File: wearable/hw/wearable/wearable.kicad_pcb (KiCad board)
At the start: 2 copper layers, 80.2 x 35 mm, 105 parts, among them IC1 LM4041CILPR, J2 Conn_02x05_Odd_Even, J3 Interrupts, J4 Data, J5 Data, J8 USBC Charger, SW1 SW_Toggle, U1 LT3042xMSE, U2 BNO080, U3 nRF54L15-QFXX, U4 MAX77659AENV+, U5 ADS1299IPAG, Y1 32MHz, Y2 32.768kHz, Y3 32.768kHz

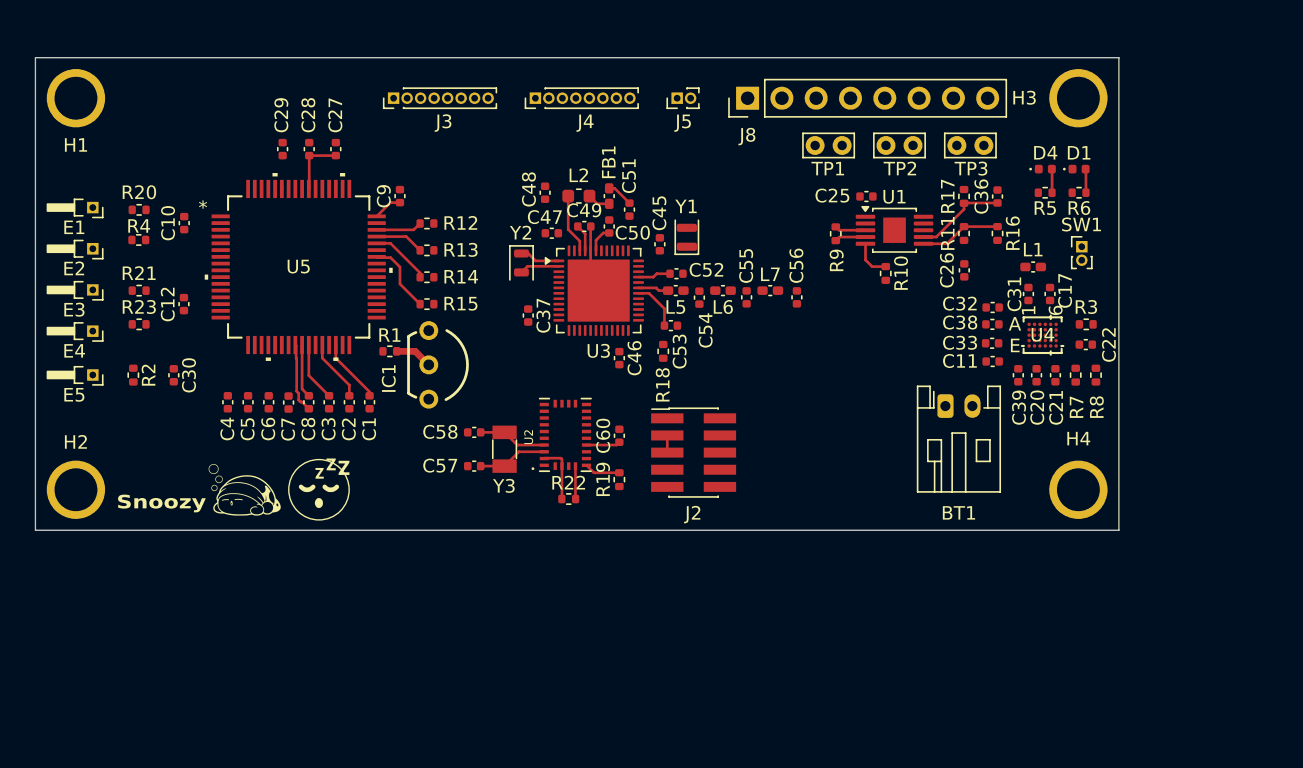
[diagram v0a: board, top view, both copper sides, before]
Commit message: Ground pours and more routing
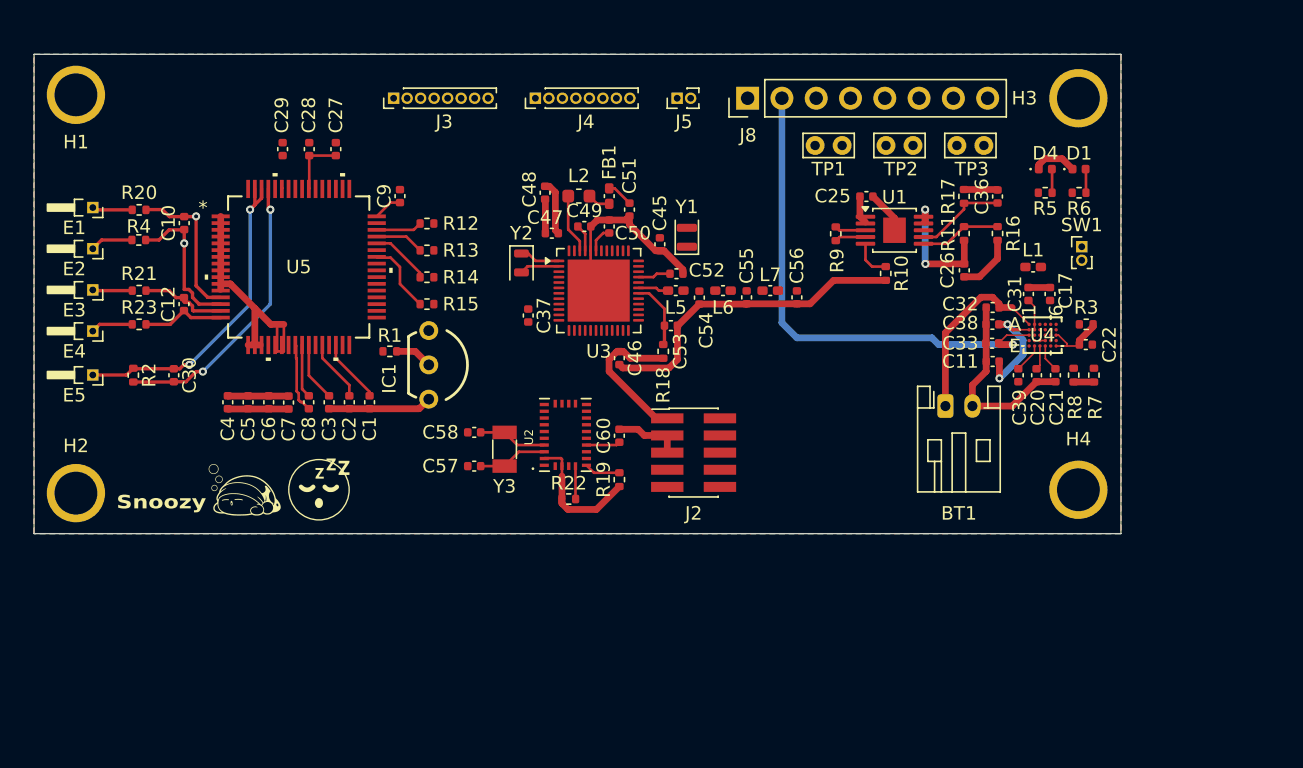
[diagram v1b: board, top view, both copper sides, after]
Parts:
- moved R8 1.65 mm to (186.5, 108.3)
- moved R7 1.35 mm to (188.0, 108.3)
- moved H1 0.25 mm to (112.6, 87.5)
- moved H2 0.25 mm to (112.6, 117.0)
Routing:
- net AVSS: track 6.88 -> 89.9 mm
- net +5V_USB: track 0.00 -> 38.0 mm, vias 0 -> 1
- net AVDD: track 0.20 -> 29.3 mm, vias 0 -> 2
- net +3V3: track 6.45 -> 33.7 mm
- net Net-(U5-BIASIN): track 0.00 -> 24.4 mm, vias 0 -> 2
- net Net-(U5-BIASINV): track 0.00 -> 21.1 mm, vias 0 -> 2
- net Net-(BT1-+): track 0.00 -> 13.7 mm
- net Net-(U5-IN2N): track 0.00 -> 11.3 mm, vias 0 -> 1
- net Net-(U5-IN2P): track 0.00 -> 11.0 mm, vias 0 -> 1
- net VSYS: track 0.00 -> 8.97 mm, vias 0 -> 2
- net Net-(U5-IN1N): track 0.00 -> 6.50 mm
- net Net-(U5-IN1P): track 0.00 -> 6.17 mm
- net +5V3: track 0.00 -> 3.86 mm
- net Net-(E2-Pad1): track 0.00 -> 3.16 mm
- net Net-(E4-Pad1): track 0.00 -> 3.13 mm
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- added copper zone on F.Cu, net AVDD
- added copper zone on B.Cu, net AVSS
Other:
- board size 80.2 x 35 mm -> 80.5 x 35.5 mm

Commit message: Significant layout progress
NOTE: We will need to rework the power management portion of the schematic due to layout issues
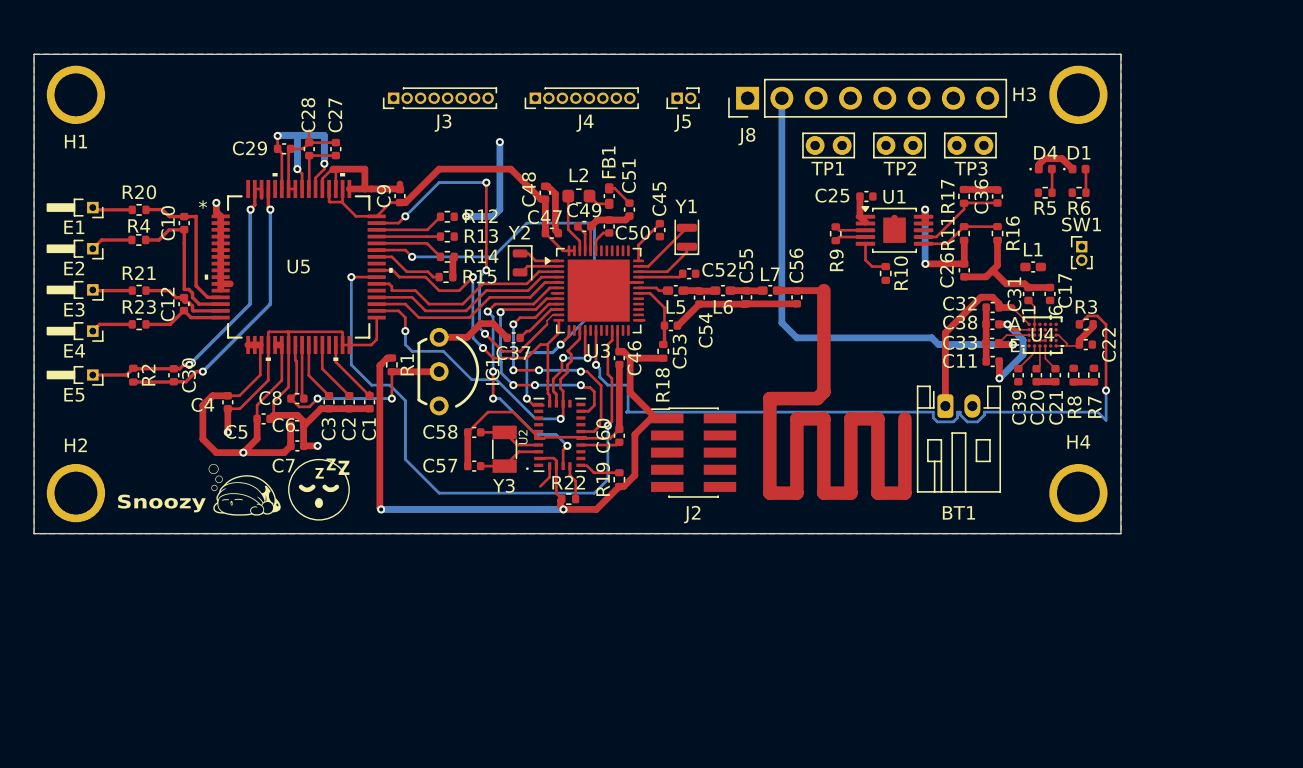
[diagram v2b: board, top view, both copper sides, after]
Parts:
- moved C7 3.28 mm to (129.0, 113.5), turned to 0 degrees
- moved C6 2.72 mm to (129.0, 112.0), turned to 0 degrees
- moved R15 2.45 mm to (140.0, 101.0)
- moved R14 2.14 mm to (140.1, 99.5)
- moved C37 1.98 mm to (145.0, 105.5), turned to 180 degrees
- moved R13 1.82 mm to (140.1, 98.0)
- moved C5 1.68 mm to (126.5, 111.5), turned to 0 degrees
- moved R12 1.59 mm to (140.1, 96.5)
- moved C45 1.05 mm to (155.8, 97.5)
- moved R1 1.01 mm to (136.0, 107.5), turned to -90 degrees
- moved C52 0.94 mm to (158.0, 100.8)
- moved IC1 0.91 mm to (139.5, 108.0)
- moved C8 0.89 mm to (129.0, 110.0), turned to 0 degrees
- moved U2 0.41 mm to (148.4, 112.7)
- moved H3 0.25 mm to (186.8, 87.5)
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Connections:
- J3 pad 3: WAKE_BNO085 -> unconnected-(J3-Pin_3-Pad3)
- U3 pad 7: WAKE_BNO085 -> unconnected-(U3-P1.06-Pad7)
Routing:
- net +3V3: track 33.7 -> 93.6 mm, vias 0 -> 2
- net RF: track 0.00 -> 59.6 mm
- net nIRQ: track 0.00 -> 55.4 mm, vias 0 -> 2
- net AVSS: track 89.9 -> 138.4 mm, vias 0 -> 4
- net CS_ADS1299: track 0.00 -> 45.7 mm, vias 0 -> 2
- net MISO: track 0.00 -> 38.3 mm, vias 0 -> 3
- net AVDD: track 29.3 -> 61.9 mm, vias 2 -> 7
- net DRDY: track 0.00 -> 28.2 mm, vias 0 -> 4
- net SCK: track 0.00 -> 25.8 mm, vias 0 -> 2
- net MOSI: track 0.00 -> 25.6 mm, vias 0 -> 2
- net BOOT_BNO085: track 0.00 -> 21.2 mm, vias 0 -> 4
- net RST_BNO085: track 0.00 -> 19.0 mm, vias 0 -> 4
- net INT_BNO085: track 0.00 -> 18.9 mm, vias 0 -> 4
- net START_ADS1299: track 0.00 -> 15.3 mm
- net PWDWN_ADS1299: track 0.00 -> 15.0 mm
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- added copper zone on B.Cu, net AVDD
- added copper zone on F.Cu, net AVSS
- removed copper zone on F.Cu, net AVDD
- removed copper zone on B.Cu, net AVSS

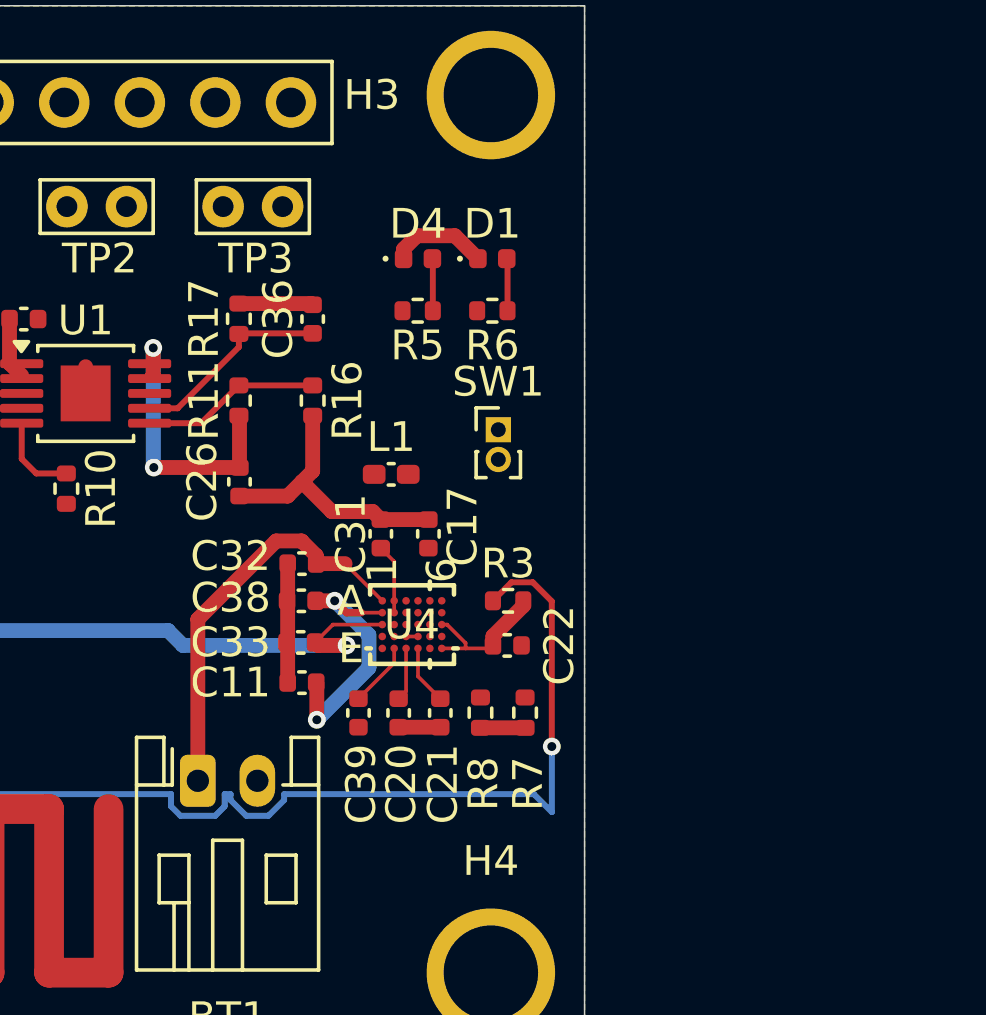
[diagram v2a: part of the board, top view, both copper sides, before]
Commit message: Schematic of new power setup done
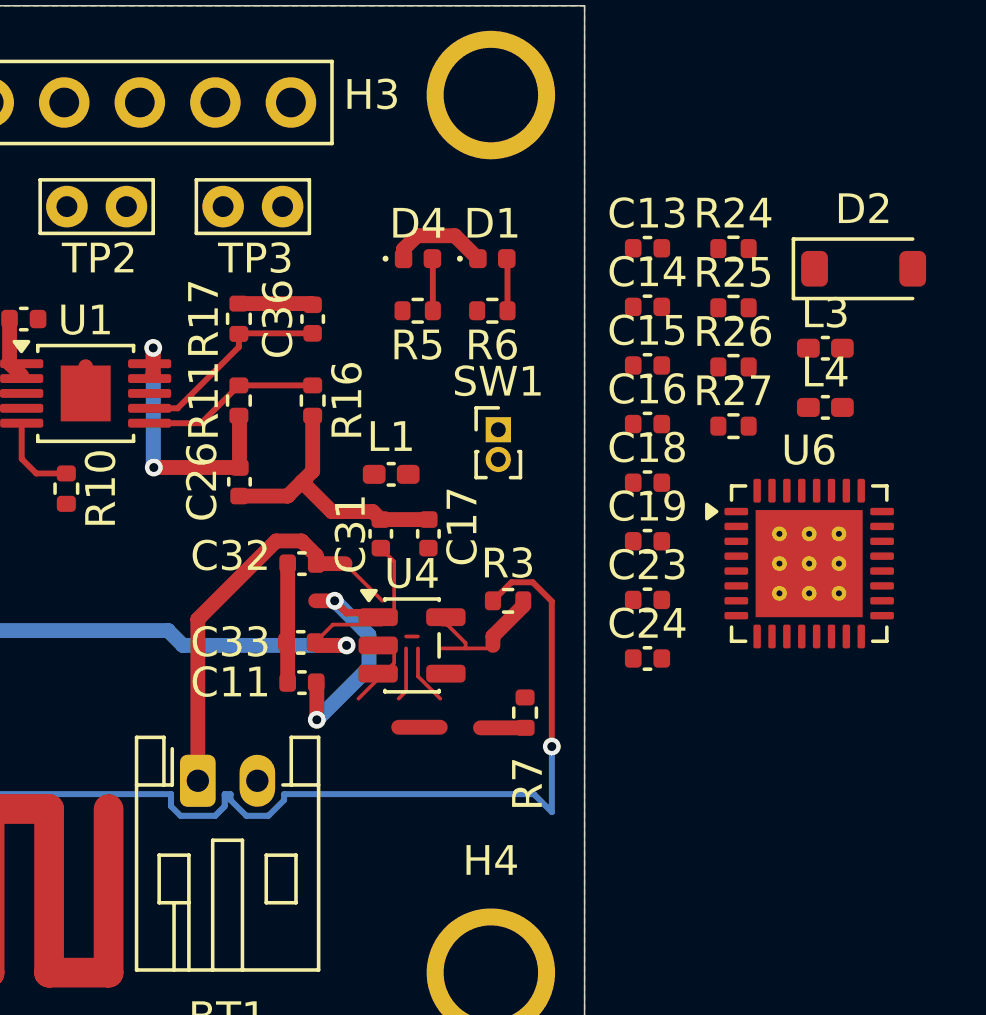
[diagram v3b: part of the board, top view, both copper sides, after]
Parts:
- removed C20, C22, C38: 22uF, Capacitor_SMD:C_0402_1005Metric
- removed C21: 1uF, Capacitor_SMD:C_0402_1005Metric
- removed C39: 10nF, Capacitor_SMD:C_0402_1005Metric
- removed R8: 10k, Resistor_SMD:R_0402_1005Metric
- added C13: 2.2uF, Capacitor_SMD:C_0402_1005Metric, F.Cu at (192.1, 92.7)
- added C14: 10uF, Capacitor_SMD:C_0402_1005Metric, F.Cu at (192.1, 94.6)
- added C15: 10uF, Capacitor_SMD:C_0402_1005Metric, F.Cu at (192.1, 96.6)
- added C16: 10uF, Capacitor_SMD:C_0402_1005Metric, F.Cu at (192.1, 98.6)
- added C18: 10uF, Capacitor_SMD:C_0402_1005Metric, F.Cu at (192.1, 100.5)
- added C19: 10uF, Capacitor_SMD:C_0402_1005Metric, F.Cu at (192.1, 102.5)
- added C23: 10uF, Capacitor_SMD:C_0402_1005Metric, F.Cu at (192.1, 104.5)
- added C24: 10uF, Capacitor_SMD:C_0402_1005Metric, F.Cu at (192.1, 106.4)
- added D2: MBR0530, Diode_SMD:D_SOD-123, F.Cu at (199.4, 93.3)
- added L3: 2.2uH, Inductor_SMD:L_0402_1005Metric_Pad0.77x0.64mm_HandSolder, F.Cu at (198.1, 96.0)
- added L4: 2.2uH, Inductor_SMD:L_0402_1005Metric_Pad0.77x0.64mm_HandSolder, F.Cu at (198.1, 98.0)
- added R24: 47k, Resistor_SMD:R_0402_1005Metric, F.Cu at (195.0, 92.7)
- added R25: 150k, Resistor_SMD:R_0402_1005Metric, F.Cu at (195.0, 94.7)
- added R26: 10k, Resistor_SMD:R_0402_1005Metric, F.Cu at (195.0, 96.6)
- added R27: 10k, Resistor_SMD:R_0402_1005Metric, F.Cu at (195.0, 98.6)
- added U6: nPM1300-QEXX, Package_DFN_QFN:QFN-32-1EP_5x5mm_P0.5mm_EP3.6x3.6mm_ThermalVias, F.Cu at (197.6, 103.2)
- C11: value 22uF -> 4.7uF
- C17: value 1uF -> 4.7uF
- C31: value 1uF -> 10uF
- C32: value 4.7uF -> 10uF
- C33: value 47uF -> 10uF
- L1: value 1.5uH -> 6.8uH
- R3: value 100K -> 698k
- R7: value 10k -> 200K
- U4: value MAX77659AENV+ -> TPS61040DBV; footprint MAX77659AENV+:21-100509_N302D2&plus_1_MXM -> Package_TO_SOT_SMD:SOT-23-5
- moved U4 0.70 mm to (184.2, 106.0)
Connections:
- C11 pad 1: VSYS -> +3V3
- C17 pad 1: Net-(U4-SBB2) -> +5V3
- C31 pad 1: Net-(U4-AVL) -> +3V3
- C32 pad 1: Net-(BT1-+) -> +3V3
- C33 pad 1: AVSS -> +3V3
- C33 pad 2: +5V_USB -> AVSS
- L1 pad 1: Net-(C39-Pad2) -> +3V3
- L1 pad 2: Net-(L1-Pad2) -> Net-(D2-A)
- R3 pad 1: nIRQ -> +5V3
- R3 pad 2: +3V3 -> Net-(U4-FB)
- R7 pad 1: SDA -> Net-(U4-FB)
- R7 pad 2: +3V3 -> AVSS
- SW1 pad 2: Net-(U4-NEN) -> Net-(U6-NTC)
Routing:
- net Net-(U4-FB): track 0.00 -> 2.19 mm
- net Net-(U4-BST): track 2.19 -> 0.00 mm
- net AVSS: track 138.4 -> 139.9 mm
- net +3V3: track 93.6 -> 92.1 mm, vias 2 -> 4
- net VSYS: vias 2 -> 0

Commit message: Slop layout for new power block
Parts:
- added C20: 3.3pF, Capacitor_SMD:C_0402_1005Metric, F.Cu at (183.0, 109.5)
- moved C15 54.8 mm to (137.5, 100.9), turned to 90 degrees
- moved C13 53.6 mm to (157.5, 133.6), turned to 90 degrees
- moved L3 36.3 mm to (162.0, 100.1), turned to 90 degrees
- moved C23 35.2 mm to (158.5, 94.0), turned to 180 degrees
- moved U6 35.2 mm to (163.2, 95.5), turned to 90 degrees
- moved C18 35.1 mm to (158.0, 92.5), turned to -90 degrees
- moved L4 34.7 mm to (163.5, 100.0), turned to 90 degrees
- moved C19 34.4 mm to (158.5, 95.5), turned to 180 degrees
- moved C16 33.7 mm to (159.0, 92.5), turned to -90 degrees
- moved C14 32.1 mm to (160.5, 100.0), turned to 90 degrees
- moved R24 27.6 mm to (167.5, 94.5), turned to -90 degrees
- moved R25 27.6 mm to (167.5, 96.5)
- moved R26 27.5 mm to (167.5, 97.5)
- moved R27 27.5 mm to (167.5, 99.5)
- moved C24 25.1 mm to (169.5, 95.5), turned to -90 degrees
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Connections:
- J3 pad 8: nIRQ -> unconnected-(J3-Pin_8-Pad8)
- U3 pad 14: unconnected-(U3-P2.03-Pad14) -> GPIO4
- U3 pad 17: unconnected-(U3-P2.06-Pad17) -> GPIO0
- U3 pad 18: nIRQ -> GPIO1
- U3 pad 19: unconnected-(U3-P2.08-Pad19) -> GPIO2
- U3 pad 20: unconnected-(U3-P2.09-Pad20) -> GPIO3
- U3 pad 23: GPIO0 -> unconnected-(U3-P0.00-Pad23)
- U3 pad 24: GPIO1 -> unconnected-(U3-P0.01-Pad24)
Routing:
- net nIRQ: track 55.4 -> 0.00 mm, vias 2 -> 0
- net +5V_USB: track 38.0 -> 8.76 mm, vias 1 -> 0
- net +3V3: track 92.1 -> 111.2 mm
- net Net-(BT1-+): track 13.7 -> 0.00 mm
- net VSYS: track 8.97 -> 0.00 mm
- net GPIO1: track 0.00 -> 8.06 mm, vias 0 -> 1
- net +5V3: track 3.86 -> 8.91 mm
- net Net-(D2-A): track 0.00 -> 4.84 mm
- net AVSS: track 139.9 -> 135.1 mm
- net Net-(U4-FB): track 2.19 -> 5.36 mm
- net Net-(U4-AVL): track 2.36 -> 0.00 mm
- net Net-(U4-SBB1): track 2.00 -> 0.00 mm
- net Net-(U1-EN/UV): track 2.30 -> 1.68 mm
- net Net-(U1-PG): track 2.31 -> 1.69 mm

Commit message: Questioning life choices
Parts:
- removed J3: Interrupts, Connector_PinHeader_1.00mm:PinHeader_1x08_P1.00mm_Vertical
- removed J4: Data, Connector_PinHeader_1.00mm:PinHeader_1x08_P1.00mm_Vertical
- removed J5: Data, Connector_PinHeader_1.00mm:PinHeader_1x02_P1.00mm_Vertical
- removed TP3: BatteryStatus, TestPoint:TestPoint_Bridge_Pitch2.0mm_Drill0.7mm
- moved TP2 55.2 mm to (117.5, 88.0)
- moved TP1 44.5 mm to (123.0, 88.0)
- moved C13 44.3 mm to (168.0, 90.5)
- moved C15 32.1 mm to (169.6, 99.8)
- moved D1 28.4 mm to (159.0, 87.8)
- moved D4 28.4 mm to (156.5, 87.8)
- moved R6 28.4 mm to (159.0, 89.5)
- moved R5 28.4 mm to (156.5, 89.5)
- moved C32 24.7 mm to (184.4, 97.4), turned to 0 degrees
- moved C33 20.9 mm to (181.9, 97.3), turned to 180 degrees
- moved R7 11.1 mm to (175.5, 106.0), turned to -90 degrees
- moved SW1 10.3 mm to (186.5, 109.0), turned to 180 degrees
- moved C20 9.92 mm to (175.5, 103.0), turned to -90 degrees
- moved C11 9.81 mm to (179.0, 108.5), turned to 180 degrees
- moved C26 8.49 mm to (185.8, 96.4)
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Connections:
- U3 pad 14: GPIO4 -> MOSI
- U3 pad 15: MOSI -> GPIO0
- U3 pad 16: CS_BNO085 -> GPIO1
- U3 pad 17: GPIO0 -> GPIO2
- U3 pad 18: GPIO1 -> GPIO3
- U3 pad 19: GPIO2 -> GPIO4
- U3 pad 20: GPIO3 -> CS_BNO085
- U3 pad 29: AMUX -> unconnected-(U3-P0.04-Pad29)
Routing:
- net AVSS: track 135.1 -> 244.9 mm, vias 4 -> 6
- net +3V3: track 111.2 -> 182.2 mm, vias 4 -> 5
- net GPIO0: track 0.00 -> 43.2 mm, vias 0 -> 3
- net GPIO2: track 0.00 -> 40.7 mm, vias 0 -> 3
- net GPIO3: track 0.00 -> 39.4 mm, vias 0 -> 3
- net GPIO4: track 0.00 -> 39.1 mm, vias 0 -> 3
- net Net-(U6-NTC): track 0.00 -> 34.2 mm, vias 0 -> 2
- net GPIO1: track 8.06 -> 41.9 mm, vias 1 -> 3
- net SWDCLK: track 0.43 -> 19.7 mm, vias 0 -> 2
- net SWDIO: track 0.00 -> 15.4 mm, vias 0 -> 2
- net RESET: track 5.12 -> 20.0 mm
- net VDDIO: track 0.00 -> 12.0 mm
- net RST_BNO085: track 19.0 -> 7.39 mm, vias 4 -> 1
- net Net-(U6-VOUT2): track 0.00 -> 10.3 mm
- net +5V3: track 8.91 -> 18.9 mm, vias 0 -> 2
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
